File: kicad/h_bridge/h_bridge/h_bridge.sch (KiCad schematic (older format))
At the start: 48 parts, among them J1 Conn_01x04_Male, J2 voltage_in, J3 motor, Q1 IRF3205, Q2 IRF3205, Q3 IRF3205, Q4 IRF3205, Q5 IRF3205, Q6 IRF3205, Q7 IRF3205, Q8 IRF3205, U1 PC123, U2 PC123, U3 74HC14, U4 L7805, U5 IR2184, U6 IR2184

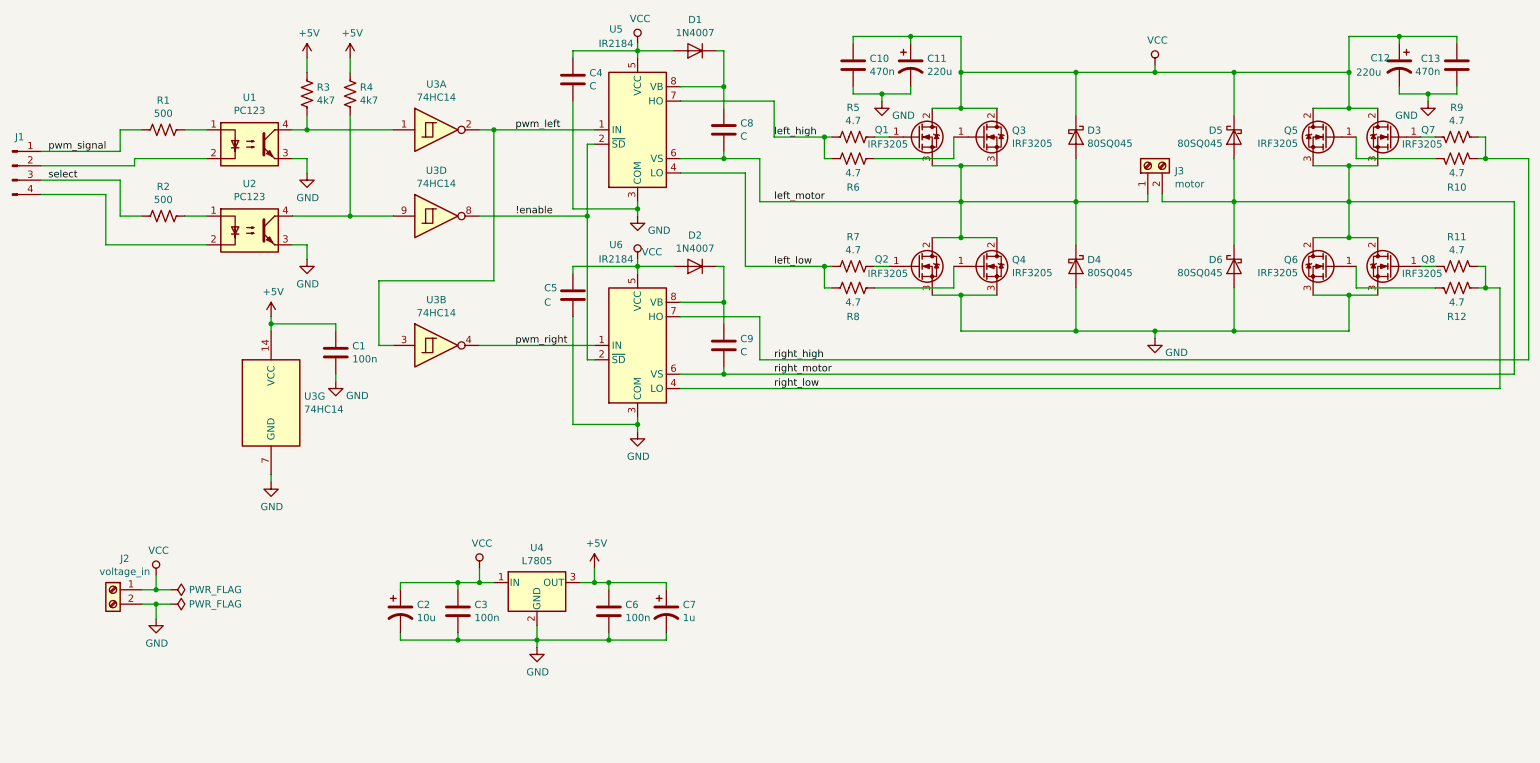
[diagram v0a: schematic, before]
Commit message: [kicad/h_bridge] schematic changed ir2184 to ir21844
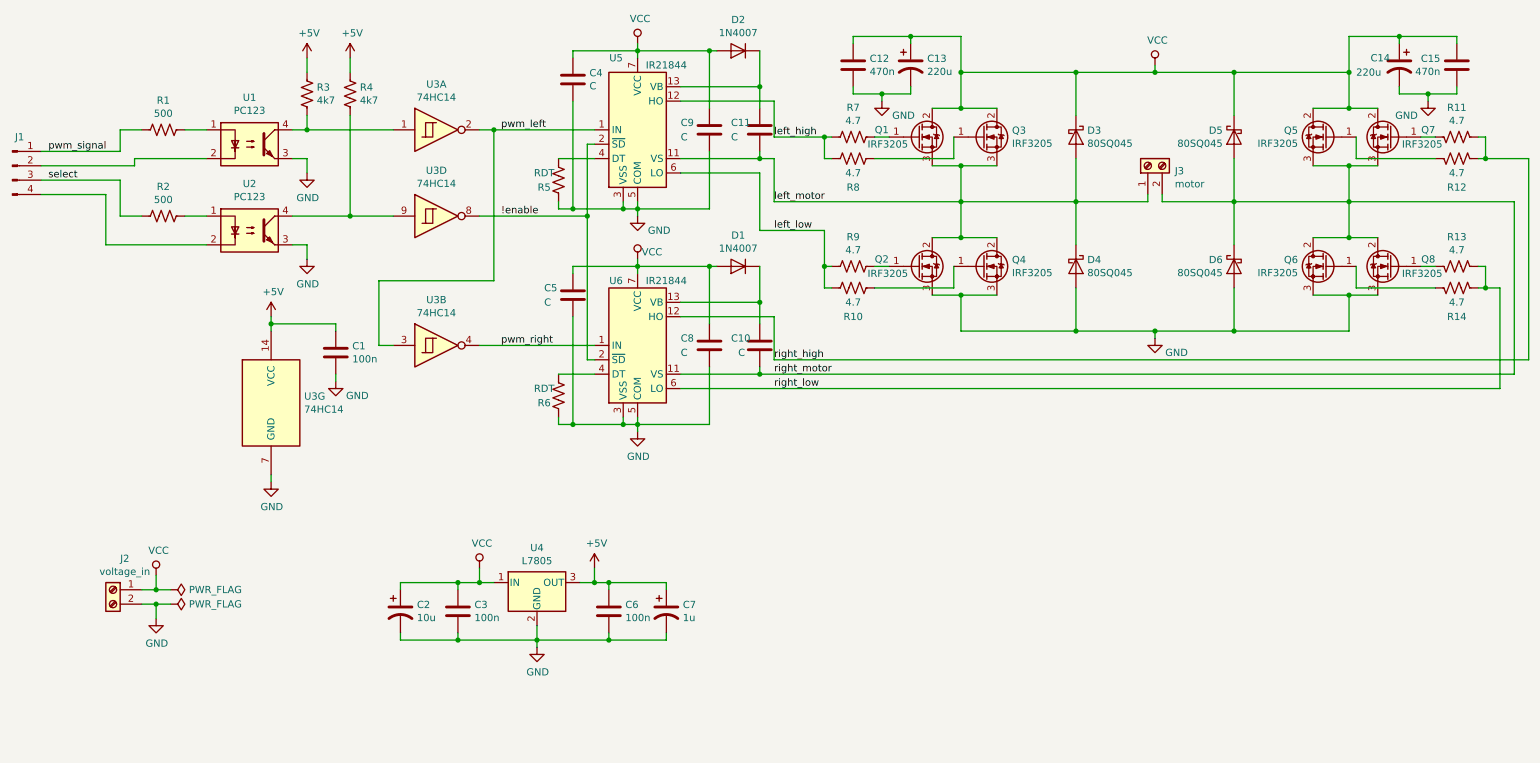
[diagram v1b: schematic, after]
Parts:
- removed U5, U6: IR2184, symbol Driver_FET:IR2184
- added C8, C9: C, Capacitor_SMD:C_0805_2012Metric, symbol Device:C
- added R5, R6: RDT, Resistor_SMD:R_0805_2012Metric, symbol Device:R_US
- added U5, U6: IR21844, Package_DIP:DIP-14_W7.62mm_LongPads, symbol Driver_FET:IR21844
- C12: renamed from C10; footprint (none) -> Capacitor_THT:C_Rect_L13.0mm_W5.0mm_P10.00mm_FKS3_FKP3_MKS4
- C13: renamed from C11; footprint (none) -> Capacitor_THT:CP_Radial_D10.0mm_P5.00mm_P7.50mm
- C14: renamed from C12; footprint (none) -> Capacitor_THT:CP_Radial_D10.0mm_P5.00mm_P7.50mm
- C15: renamed from C13; footprint (none) -> Capacitor_THT:C_Rect_L13.0mm_W5.0mm_P10.00mm_FKS3_FKP3_MKS4
- C2, C7: footprint (none) -> Capacitor_THT:CP_Radial_D5.0mm_P2.50mm
- D3, D4, D5, D6: footprint (none) -> Diode_THT:D_DO-201AD_P12.70mm_Horizontal
- J1: footprint (none) -> Connector_PinHeader_2.54mm:PinHeader_1x04_P2.54mm_Vertical
- J2, J3: footprint (none) -> Connector_Wire:SolderWirePad_1x02_P7.62mm_Drill2.5mm
- U3: footprint (none) -> Package_DIP:DIP-14_W7.62mm_LongPads
- U4: footprint (none) -> Package_TO_SOT_THT:TO-220-3_Vertical
- renumbered C9 to C10, C8 to C11, D2 to D1, D1 to D2, R8 to R10, R9 to R11, R10 to R12, R11 to R13, R12 to R14, R5 to R7, R6 to R8, R7 to R9
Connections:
- net !enable: now also U5.2 (~SD), U6.2 (~SD)
- net GND: now also C8.2, C9.2, R5.1, R6.1, U5.3 (VSS), U5.5 (COM), U6.3 (VSS), U6.5 (COM)
- net VCC: now also C8.1, C9.1, U5.7 (VCC), U6.7 (VCC)
- net left_high: now also U5.12 (HO)
- net left_low: now also U5.6 (LO)
- net left_motor: now also U5.11 (VS)
- net pwm_left: now also U5.1 (IN)
- net pwm_right: now also U6.1 (IN)
- net right_high: now also U6.12 (HO)
- net right_low: now also U6.6 (LO)
- net right_motor: now also U6.11 (VS)
- net at C11.1, D2.1 (K): now also U5.13 (VB)
- net at C10.1, D1.1 (K): now also U6.13 (VB)
- new net: R5.2, U5.4 (DT)
- new net: R6.2, U6.4 (DT)
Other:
- moved on the sheet: C10, C11, D1, D2

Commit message: [kicad/h_bridge] schematic changed voltage regutlator to lm317
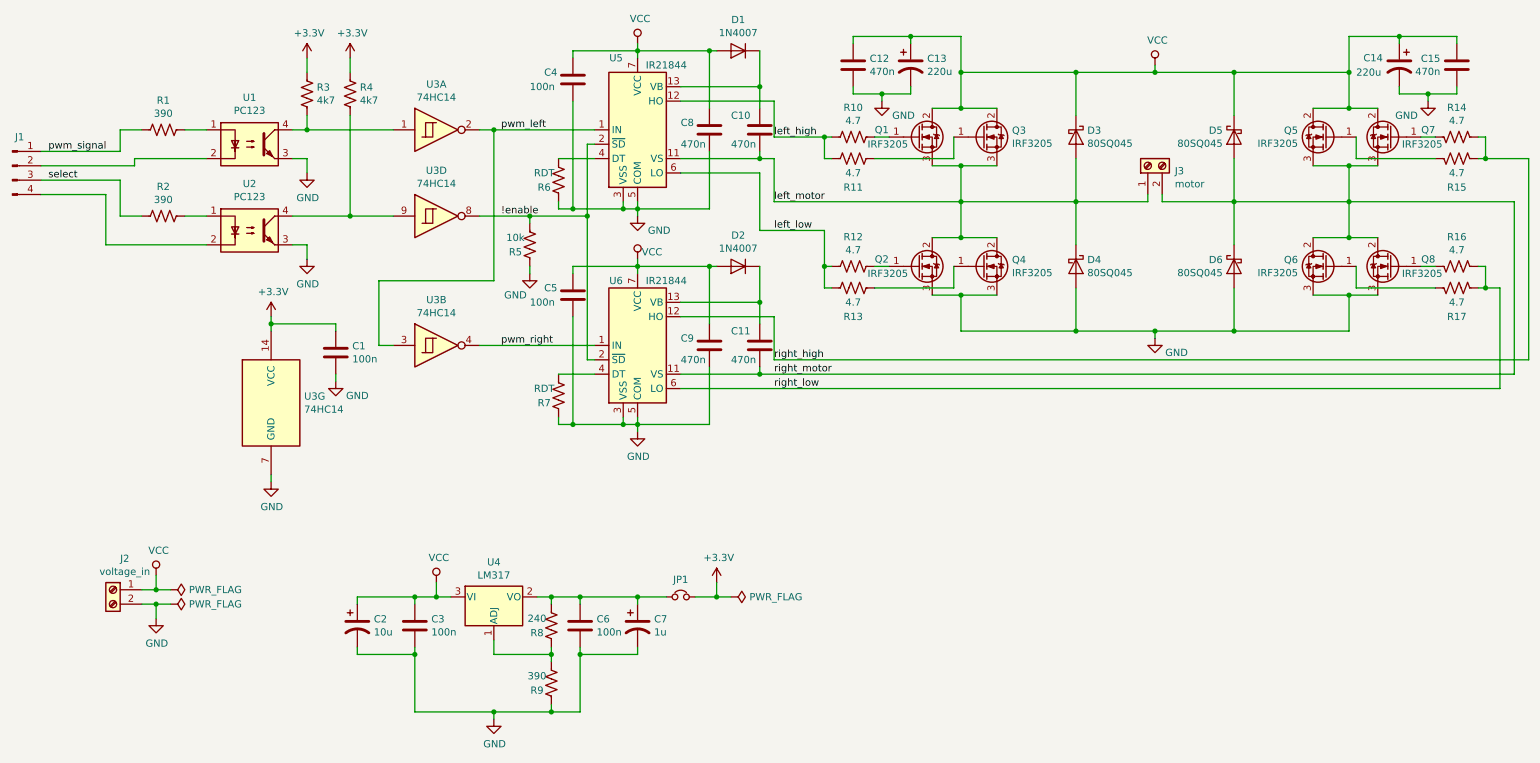
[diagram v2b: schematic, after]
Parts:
- removed U4: L7805, Package_TO_SOT_THT:TO-220-3_Vertical, symbol Regulator_Linear:L7805
- added JP1: Jumper_NC_Small, Connector_PinHeader_2.54mm:PinHeader_1x02_P2.54mm_Vertical, symbol Device:Jumper_NC_Small
- added R5: 10k, Resistor_SMD:R_0805_2012Metric, symbol Device:R_US
- added R8: 240, Resistor_SMD:R_0805_2012Metric, symbol Device:R_US
- added R9: 390, Resistor_SMD:R_0805_2012Metric, symbol Device:R_US
- added U4: LM317, Package_TO_SOT_THT:TO-220-3_Horizontal_TabDown, symbol Regulator_Linear:LM317_3PinPackage
- C10: renamed from C11; value C -> 470n
- C11: renamed from C10; value C -> 470n
- C4, C5: value C -> 100n
- C8: renamed from C9; value C -> 470n
- C9: renamed from C8; value C -> 470n
- R1, R2: value 500 -> 390
- renumbered D2 to D1, D1 to D2, R7 to R10, R8 to R11, R9 to R12, R10 to R13, R11 to R14, R12 to R15, R13 to R16, R14 to R17, R5 to R6, R6 to R7
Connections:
- net !enable: now also R5.2
- net GND: now also R5.1, R9.1
- net VCC: now also U4.3 (VI)
- net +5V renamed +3V3
- net +3V3: now also JP1.2; no longer C6.1, C7.1
- new net: R8.1, R9.2, U4.1 (ADJ)
- new net: C6.1, C7.1, JP1.1, R8.2, U4.2 (VO)
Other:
- moved on the sheet: C2, C3, C6, C7

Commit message: [kicad/h_bridge] layout basically done; vias on the edge are missing; testing need to be done
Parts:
- removed unit 4 of U3
- added unit 3 of U3
- C13, C14: footprint Capacitor_THT:CP_Radial_D10.0mm_P5.00mm_P7.50mm -> Capacitor_THT:CP_Radial_D10.0mm_P5.00mm
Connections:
- net !enable: now also U3.6
- net at R4.1, U2.4: now also U3.5
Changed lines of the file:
@@
-	1    0    0    -1
-$EndComp
-$Comp
-L 74xx:74HC14 U3
-U 4 1 5E92CBC5
-P 3500 2550
-F 0 "U3" H 3500 2867 50  0000 C CNN
-F 1 "74HC14" H 3500 2776 50  0000 C CNN
-F 2 "Package_DIP:DIP-14_W7.62mm_LongPads" H 3500 2550 50  0001 C CNN
-F 3 "http://www.ti.com/lit/gpn/sn74HC14" H 3500 2550 50  0001 C CNN
-	4    3500 2550
 	1    0    0    -1
 $EndComp
@@
 F 0 "C13" H 6915 1546 50  0000 L CNN
 F 1 "220u" H 6915 1455 50  0000 L CNN
-F 2 "Capacitor_THT:CP_Radial_D10.0mm_P5.00mm_P7.50mm" H 6800 1500 50  0001 C CNN
+F 2 "Capacitor_THT:CP_Radial_D10.0mm_P5.00mm" H 6800 1500 50  0001 C CNN
 F 3 "~" H 6800 1500 50  0001 C CNN
 	1    6800 1500
@@
 F 0 "C14" H 10450 1550 50  0000 R CNN
 F 1 "220u" H 10500 1450 50  0000 R CNN
-F 2 "Capacitor_THT:CP_Radial_D10.0mm_P5.00mm_P7.50mm" H 10200 1500 50  0001 C CNN
+F 2 "Capacitor_THT:CP_Radial_D10.0mm_P5.00mm" H 10200 1500 50  0001 C CNN
 F 3 "~" H 10200 1500 50  0001 C CNN
 	1    10200 1500
@@
 Wire Wire Line
 	4300 5600 4300 5650
+$Comp
+L 74xx:74HC14 U3
+U 3 1 5EEFAB55
+P 3500 2550
+F 0 "U3" H 3500 2867 50  0000 C CNN
+F 1 "74HC14" H 3500 2776 50  0000 C CNN
+F 2 "Package_DIP:DIP-14_W7.62mm_LongPads" H 3500 2550 50  0001 C CNN
+F 3 "http://www.ti.com/lit/gpn/sn74HC14" H 3500 2550 50  0001 C CNN
+	3    3500 2550
+	1    0    0    -1
+$EndComp
 $EndSCHEMATC

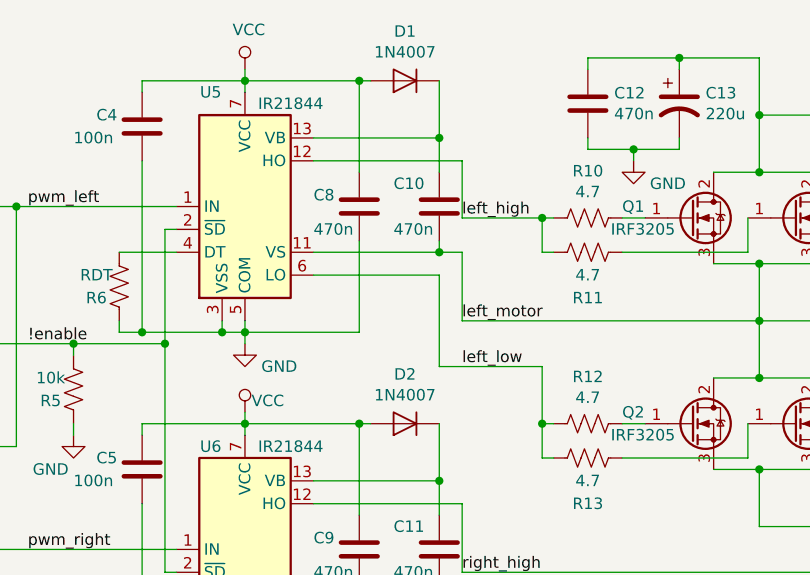
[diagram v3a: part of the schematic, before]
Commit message: [kicad/h_bridge] small changes
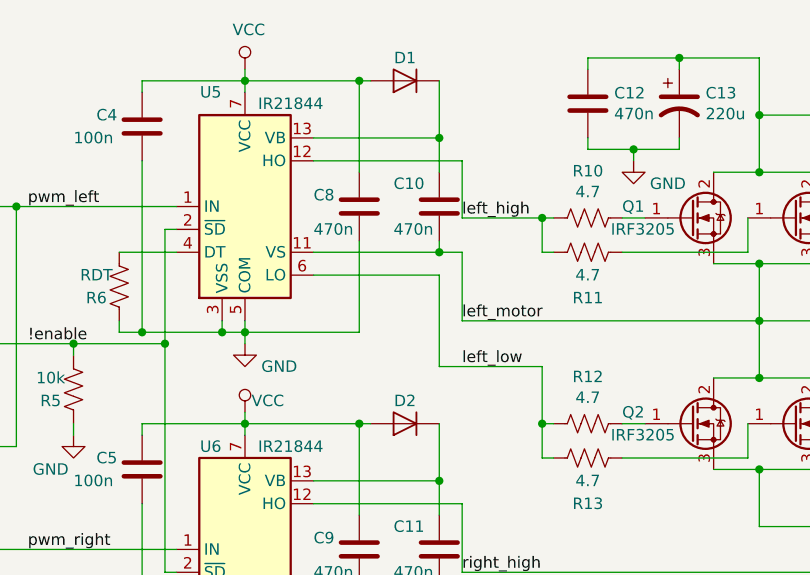
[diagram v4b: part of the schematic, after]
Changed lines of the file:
@@
 U 1 1 5E982D0F
 P 5600 2900
-F 0 "D2" H 5600 2684 50  0000 C CNN
-F 1 "1N4007" H 5600 2775 50  0000 C CNN
+F 0 "D2" H 5600 2800 50  0000 C CNN
+F 1 "1N4007" H 5600 2775 50  0001 C CNN
 F 2 "Diode_THT:D_DO-41_SOD81_P10.16mm_Horizontal" H 5600 2725 50  0001 C CNN
 F 3 "http://www.vishay.com/docs/88503/1n4001.pdf" H 5600 2900 50  0001 C CNN
@@
 U 1 1 5E984843
 P 5600 1400
-F 0 "D1" H 5600 1184 50  0000 C CNN
-F 1 "1N4007" H 5600 1275 50  0000 C CNN
+F 0 "D1" H 5600 1300 50  0000 C CNN
+F 1 "1N4007" H 5600 1275 50  0001 C CNN
 F 2 "Diode_THT:D_DO-41_SOD81_P10.16mm_Horizontal" H 5600 1225 50  0001 C CNN
 F 3 "http://www.vishay.com/docs/88503/1n4001.pdf" H 5600 1400 50  0001 C CNN
